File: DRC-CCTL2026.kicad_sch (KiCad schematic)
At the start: 46 parts, among them J1 USB_C, J10 SW3, J2 FDCAN1, J3 FDCAN2, J4 FDCAN3, J5 SW1, J6 SW2, J7 STLINK, J8 I2C, J9 USART, Q1 MMBT3904, SW1 SW_Push, SW2 DIP, U1 STM32G474RETx, U2 AZ1084C-3.3, U3 74AHCT1G125, Y1 8M10PB/XT324-10/80

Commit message: ledの抵抗値を変更
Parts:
- R3, R5: value 1k -> 470
- R4: value 2.2k -> 1k
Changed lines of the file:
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@@
 			)
 		)
-		(property "Value" "2.2k"
+		(property "Value" "1k"
 			(at 173.99 96.5199 0)
 			(effects
@@
 			)
 		)
-		(property "Value" "1k"
+		(property "Value" "470"
 			(at 184.15 96.5199 0)
 			(effects
@@
 			)
 		)
-		(property "Value" "1k"
+		(property "Value" "470"
 			(at 163.83 96.5199 0)
 			(effects

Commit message: パターン引き直し・部品配置変更
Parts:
- removed U3: 74AHCT1G125, lib:SOT95P280X145-5N, symbol 74xGxx:74AHCT1G125
- added U3: 74AHC1G125, Package_TO_SOT_SMD:SOT-353_SC-70-5, symbol 74xGxx:74AHC1G125
- C1, C2: value 12p -> 10p; footprint Capacitor_SMD:C_0603_1608Metric_Pad1.08x0.95mm_HandSolder -> Capacitor_THT:C_Disc_D5.0mm_W2.5mm_P5.00mm
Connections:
- net +5V: now also U3.5 (VCC)
- net GND: now also U3.1, U3.3 (GND)
- net RGB: now also U3.2
- net at D3.4 (DIN): now also U3.4
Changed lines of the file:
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@@
 	)
 	(symbol
-		(lib_id "74xGxx:74AHCT1G125")
+		(lib_id "power:GND")
+		(at 261.62 71.12 0)
+		(unit 1)
+		(exclude_from_sim no)
+		(in_bom yes)
+		(on_board yes)
+		(dnp no)
+		(property "Reference" "#PWR035"
+			(at 261.62 77.47 0)
+			(effects
+				(font
+					(size 1.27 1.27)
+				)
+				(hide yes)
+			)
+		)
+		(property "Value" "GND"
+			(at 261.62 76.2 0)
+			(effects
+				(font
+					(size 1.27 1.27)
+				)
+			)
+		)
+		(property "Footprint" ""
+			(at 261.62 71.12 0)
+			(effects
+				(font
+					(size 1.27 1.27)
+				)
+				(hide yes)
+			)
+		)
+		(property "Datasheet" ""
+			(at 261.62 71.12 0)
+			(effects
+				(font
+					(size 1.27 1.27)
+				)
+				(hide yes)
+			)
+		)
+		(property "Description" "Power symbol creates a global label with name \"GND\" , ground"
+			(at 261.62 71.12 0)
+			(effects
+				(font
+					(size 1.27 1.27)
+				)
+				(hide yes)
+			)
+		)
+		(pin "1"
+		)
+		(instances
+			(project "DRC-CCTL2026"
+				(path "/5b9f915a-dea8-4ee6-a342-61437447bbca"
+					(reference "#PWR035")
+					(unit 1)
+				)
+			)
+		)
+	)
+	(symbol
+		(lib_id "74xGxx:74AHC1G125")
 		(at 148.59 132.08 0)
 		(unit 1)
@@
 		(dnp no)
 		(property "Reference" "U3"
-			(at 134.112 137.922 0)
-			(effects
-				(font
-					(size 1.27 1.27)
-				)
-			)
-		)
-		(property "Value" "74AHCT1G125"
-			(at 134.112 140.462 0)
-			(effects
-				(font
-					(size 1.27 1.27)
-				)
-			)
-		)
-		(property "Footprint" "lib:SOT95P280X145-5N"
+			(at 133.858 124.714 0)
+			(effects
+				(font
+					(size 1.27 1.27)
+				)
+			)
+		)
+		(property "Value" "74AHC1G125"
+			(at 133.858 127.254 0)
+			(effects
+				(font
+					(size 1.27 1.27)
+				)
+			)
+		)
+		(property "Footprint" "Package_TO_SOT_SMD:SOT-353_SC-70-5"
 			(at 148.59 132.08 0)
 			(effects
@@
 		(pin "5"
 		)
+		(pin "1"
+		)
+		(pin "4"
+		)
+		(pin "2"
+		)
 		(pin "3"
 		)
-		(pin "4"
-		)
-		(pin "2"
-		)
-		(pin "1"
-		)
 		(instances
 			(project "DRC-CCTL2026"
 				(path "/5b9f915a-dea8-4ee6-a342-61437447bbca"
 					(reference "U3")
-					(unit 1)
-				)
-			)
-		)
-	)
-	(symbol
-		(lib_id "power:GND")
-		(at 261.62 71.12 0)
-		(unit 1)
-		(exclude_from_sim no)
-		(in_bom yes)
-		(on_board yes)
-		(dnp no)
-		(property "Reference" "#PWR035"
-			(at 261.62 77.47 0)
-			(effects
-				(font
-					(size 1.27 1.27)
-				)
-				(hide yes)
-			)
-		)
-		(property "Value" "GND"
-			(at 261.62 76.2 0)
-			(effects
-				(font
-					(size 1.27 1.27)
-				)
-			)
-		)
-		(property "Footprint" ""
-			(at 261.62 71.12 0)
-			(effects
-				(font
-					(size 1.27 1.27)
-				)
-				(hide yes)
-			)
-		)
-		(property "Datasheet" ""
-			(at 261.62 71.12 0)
-			(effects
-				(font
-					(size 1.27 1.27)
-				)
-				(hide yes)
-			)
-		)
-		(property "Description" "Power symbol creates a global label with name \"GND\" , ground"
-			(at 261.62 71.12 0)
-			(effects
-				(font
-					(size 1.27 1.27)
-				)
-				(hide yes)
-			)
-		)
-		(pin "1"
-		)
-		(instances
-			(project "DRC-CCTL2026"
-				(path "/5b9f915a-dea8-4ee6-a342-61437447bbca"
-					(reference "#PWR035")
 					(unit 1)
 				)
@@
 		(on_board yes)
 		(dnp no)
-		(fields_autoplaced yes)
 		(property "Reference" "C2"
-			(at 40.6463 135.89 90)
-			(effects
-				(font
-					(size 1.27 1.27)
-				)
-			)
-		)
-		(property "Value" "12p"
-			(at 40.6463 138.43 90)
-			(effects
-				(font
-					(size 1.27 1.27)
-				)
-			)
-		)
-		(property "Footprint" "Capacitor_SMD:C_0603_1608Metric_Pad1.08x0.95mm_HandSolder"
+			(at 40.6463 125.73 90)
+			(effects
+				(font
+					(size 1.27 1.27)
+				)
+			)
+		)
+		(property "Value" "10p"
+			(at 40.6463 128.27 90)
+			(effects
+				(font
+					(size 1.27 1.27)
+				)
+			)
+		)
+		(property "Footprint" "Capacitor_THT:C_Disc_D5.0mm_W2.5mm_P5.00mm"
 			(at 40.64 132.08 0)
 			(effects
@@
 			)
 		)
-		(property "Value" "12p"
+		(property "Value" "10p"
 			(at 40.6463 120.65 90)
 			(effects
@@
 			)
 		)
-		(property "Footprint" "Capacitor_SMD:C_0603_1608Metric_Pad1.08x0.95mm_HandSolder"
+		(property "Footprint" "Capacitor_THT:C_Disc_D5.0mm_W2.5mm_P5.00mm"
 			(at 40.64 124.46 0)
 			(effects

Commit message: CANの終端抵抗を削除、シルクスクリーンを調整
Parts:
- renumbered D6 to D2, D2 to D3, D3 to D4, D4 to D5, D5 to D6, R11 to R3, R3 to R4, R4 to R5, R5 to R6

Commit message: v0.2.0
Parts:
- removed C1, C2: 10p, Capacitor_THT:C_Disc_D5.0mm_W2.5mm_P5.00mm, symbol Device:C_Small
- removed C10, C12, C14, C15, C3, C7, C8, C9: 0.1u, Capacitor_SMD:C_0603_1608Metric_Pad1.08x0.95mm_HandSolder, symbol Device:C_Small
- removed C11, C13, C16: 1u, Capacitor_SMD:C_0603_1608Metric_Pad1.08x0.95mm_HandSolder, symbol Device:C_Small
- removed C6: 4.7u, Capacitor_SMD:C_0805_2012Metric_Pad1.18x1.45mm_HandSolder, symbol Device:C_Small
- removed D1: SS2040FL, Diode_SMD:D_SOD-123F, symbol Device:D_Schottky_Small
- removed D2: 1N4148W, Diode_SMD:D_SOD-123, symbol Diode:1N4148W
- removed D4: RGB, LED_SMD:LED_WS2812B_PLCC4_5.0x5.0mm_P3.2mm, symbol LED:WS2812B
- removed D5: 5V, LED_SMD:LED_0603_1608Metric_Pad1.05x0.95mm_HandSolder, symbol Device:LED_Small
- removed J1: USB_C, Connector_USB:USB_C_Receptacle_GCT_USB4105-xx-A_16P_TopMnt_Horizontal, symbol Connector:USB_C_Receptacle_USB2.0_16P
- removed J9: USART, Connector_JST:JST_XH_S4B-XH-A_1x04_P2.50mm_Horizontal, symbol Connector_Generic:Conn_01x04
- removed R1: 5.1k, Resistor_SMD:R_0603_1608Metric_Pad0.98x0.95mm_HandSolder, symbol lib:R_Small
- removed R5: 1k, Resistor_SMD:R_0603_1608Metric_Pad0.98x0.95mm_HandSolder, symbol lib:R_Small
- removed R6: 470, Resistor_SMD:R_0603_1608Metric_Pad0.98x0.95mm_HandSolder, symbol lib:R_Small
- removed SW1: SW_Push, Button_Switch_SMD:SW_SPST_EVQPE1, symbol Switch:SW_Push
- removed U1: STM32G474RETx, Package_QFP:LQFP-64_10x10mm_P0.5mm, symbol MCU_ST_STM32G4:STM32G474RETx
- removed U3: 74AHC1G125, Package_TO_SOT_SMD:SOT-353_SC-70-5, symbol 74xGxx:74AHC1G125
- removed Y1: 8M10PB/XT324-10/80, lib:8M10PB_XT324-10_80, symbol Device:Crystal_GND24_Small
- added D2, D3, D4: SS2040FL, Diode_SMD:D_SOD-123F, symbol Device:D_Schottky_Small
- added D5: 1N4148W, Diode_SMD:D_SOD-123, symbol Device:D_Small
- added D7: LED2, LED_SMD:LED_0603_1608Metric_Pad1.05x0.95mm_HandSolder, symbol Device:LED_Small
- added D8: LED3, LED_SMD:LED_0603_1608Metric_Pad1.05x0.95mm_HandSolder, symbol Device:LED_Small
- added J9: I2C2, Connector_JST:JST_XH_S5B-XH-A_1x05_P2.50mm_Horizontal, symbol Connector_Generic:Conn_01x05
- added R16, R17, R18, R19: 4.7k, Resistor_SMD:R_0603_1608Metric_Pad0.98x0.95mm_HandSolder, symbol lib:R_Small
- added R3, R4: 1k, Resistor_SMD:R_0603_1608Metric_Pad0.98x0.95mm_HandSolder, symbol lib:R_Small
- D6: value LED -> LED1
- J1: renamed from J7; footprint Connector_JST:JST_PH_S6B-PH-K_1x06_P2.00mm_Horizontal -> Connector_IDC:IDC-Header_2x03_P2.54mm_Vertical
- J8: value I2C -> I2C1
- R1: renamed from R4; value 470 -> 1k
- R2: value 5.1k -> 1k
- renumbered C4 to C1, C5 to C2, D3 to D1, J10 to J7, R3 to R6, SW2 to SW1, U2 to U1
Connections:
- net +3V3: now also J1.3 (Pin_3), D3.2 (A), D4.2 (A), D5.1 (K), R16.1, R17.1, R18.1, R19.1; no longer J8.2 (Pin_2)
- net +5V: now also D2.1 (K); no longer J1.2 (Pin_2)
- net GND: now also D7.1 (K), D8.1 (K), J9.1 (Pin_1); no longer R2.2
- net STM32G474/LED1: now reaches R2.1
- net at D6.2 (A): now also R2.2
- net at BZ1.2 (-), Q1.3 (C): now also D5.2 (A)
- net BUZZER renamed STM32G474/BZ_TIM1_CH4
- net DIP1 renamed STM32G474/DIP1
- net DIP2 renamed STM32G474/DIP2
- net DIP3 renamed STM32G474/DIP3
- net DIP4 renamed STM32G474/DIP4
- net I2C_INT renamed STM32G474/I2C1_INT
- net I2C_SCL renamed STM32G474/I2C1_SCL
- net STM32G474/I2C1_SCL: now also R17.2
- net I2C_SDA renamed STM32G474/I2C1_SDA
- net STM32G474/I2C1_SDA: now also R16.2
- net SW1 renamed STM32G474/SW1
- net SW2 renamed STM32G474/SW2
- net SW3 renamed STM32G474/SW3
- new net: D3.1 (K), J8.2 (Pin_2)
- new net: D2.2 (A), J1.2 (Pin_2)
- new net: D8.2 (A), R4.2
- new net: D7.2 (A), R3.2
- new net: D4.1 (K), J9.2 (Pin_2)
- new net STM32G474/I2C2_INT: J9.3 (Pin_3)
- new net STM32G474/I2C2_SCL: J9.4 (Pin_4), R19.2
- new net STM32G474/I2C2_SDA: J9.5 (Pin_5), R18.2
- new net STM32G474/LED2: R3.1
- new net STM32G474/LED3: R4.1
- no-connect marks 26 -> 0
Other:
- sheet AQM1602Y_LCD renamed LCD
- added sheet STM32G474 (STM32G474RET.kicad_sch)
- added sheet USBC1 (USBC_UART.kicad_sch)
- added sheet USBC2 (USBC_UART.kicad_sch)
- sheet LCD ports: added none; removed LCD_RES
- note removed: "Need to set Option Bytes"
- moved on the sheet: BZ1, C1, C2, D1, J1, J2, J3, J4, J5, J6, J7, J8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

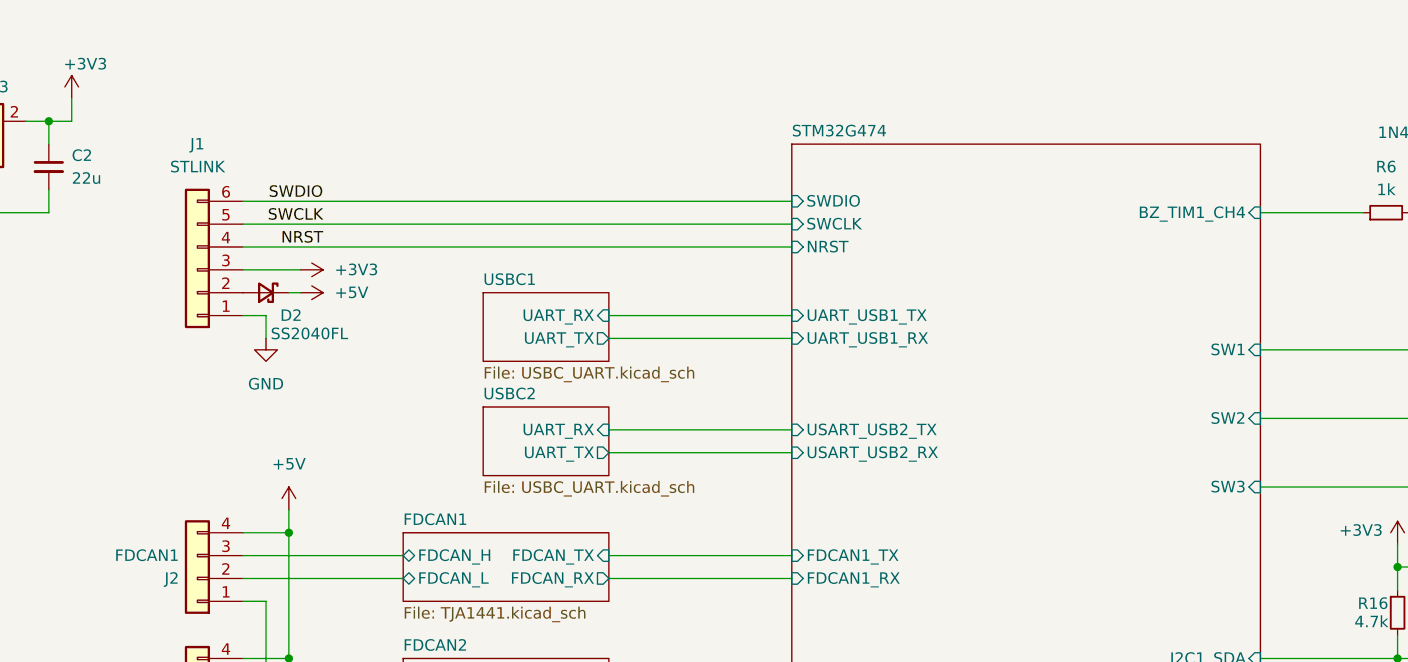
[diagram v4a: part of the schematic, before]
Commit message: v0.2.1, USB CDC に対応
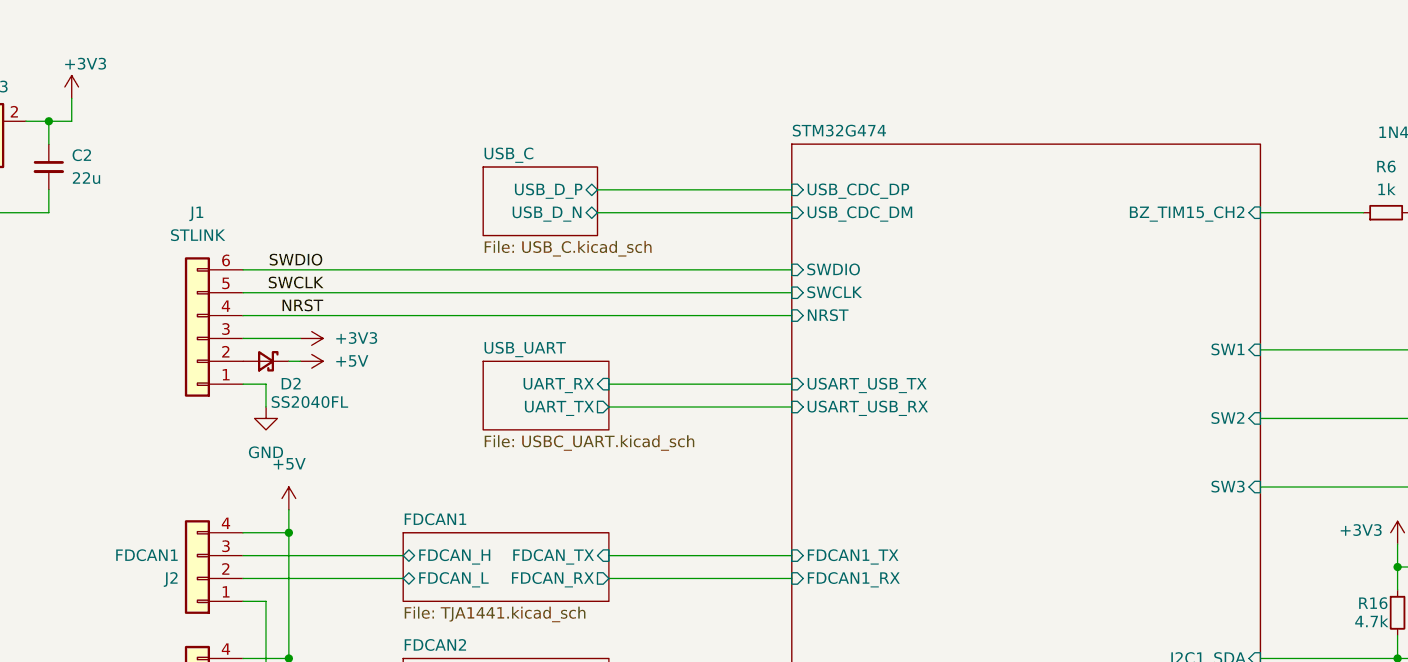
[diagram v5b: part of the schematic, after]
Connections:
- net STM32G474/BZ_TIM1_CH4 renamed STM32G474/BZ_TIM15_CH2
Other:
- sheet USBC1 renamed USB_UART
- removed sheet USBC2
- added sheet USB_C (USB_C.kicad_sch)
- sheet STM32G474 ports: added BZ_TIM15_CH2, USART_USB_RX, USART_USB_TX, USB_CDC_DM, USB_CDC_DP; removed BZ_TIM1_CH4, UART_USB1_RX, UART_USB1_TX, USART_USB2_RX, USART_USB2_TX
- moved on the sheet: D2, J1
